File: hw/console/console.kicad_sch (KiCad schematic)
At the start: 155 parts, among them J1 Batt, J301 USB-C 16P, J401 DM3AT-SF-PEJM5, J501 SPK 8R, J601 FFC-40 0.5mm, J901 UART, Q601 AO3400A, SW1 Движок, SW101 UP, SW102 DOWN, SW103 LEFT, SW104 RIGHT, SW105 SELECT, SW106 START, SW107 A, SW108 B, SW109 C, SW110 D, U1 F133-A, U2 SY8089AAAC, U3 SY8089AAAC, U4 SY8089AAAC, U401 W25Q32JVSSIQ, U5 TP4056, U501 PAM8301, Y1 24 МГц, Y2 32.768 кГц

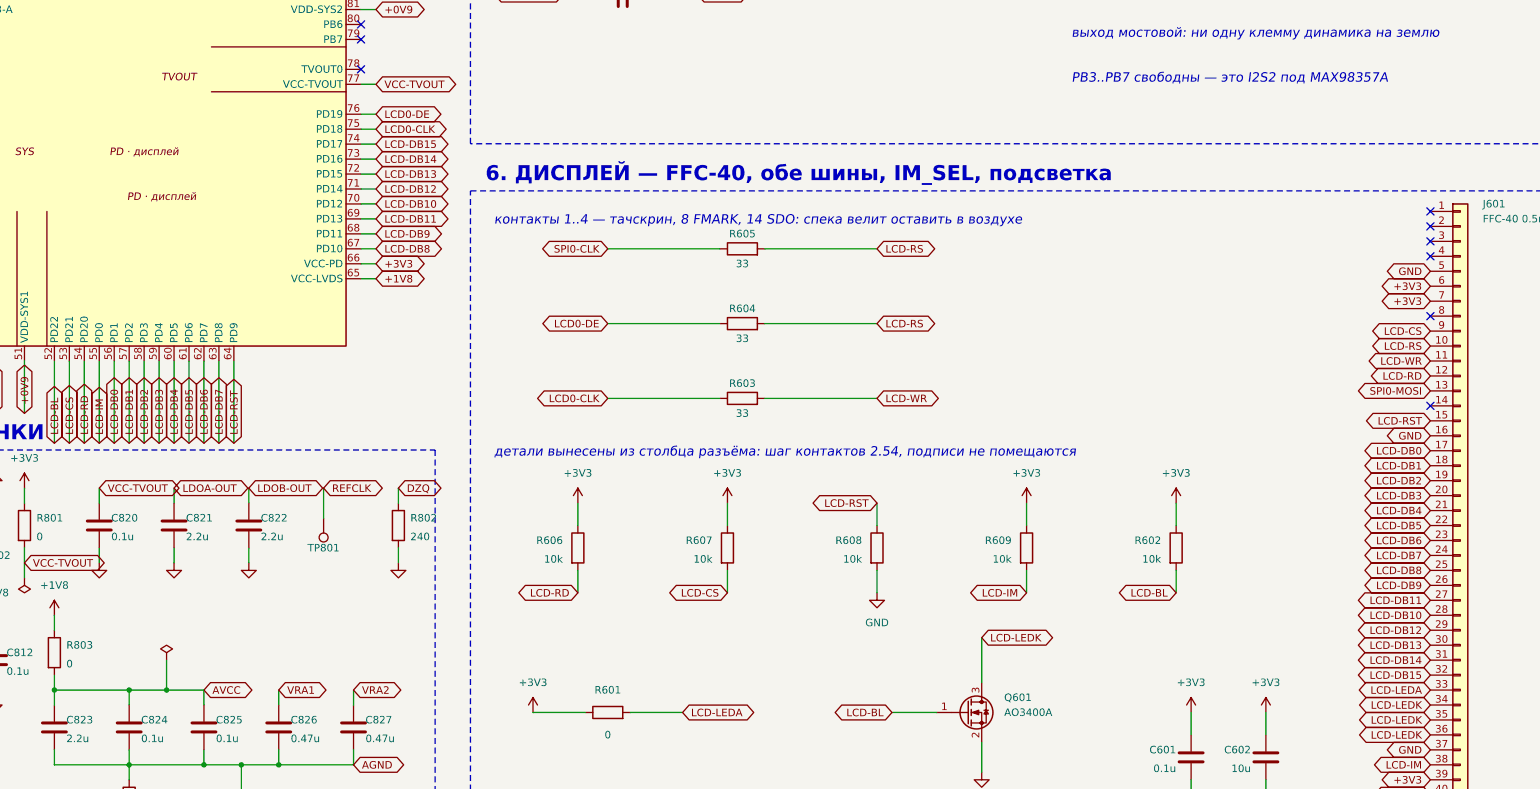
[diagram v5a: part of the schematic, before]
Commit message: hw: дисплей только по SPI — и такт приходил не на тот вывод
Главное: в `06-display.md §2.2` выводы 10 и 11 шлейфа были перепутаны, схема
KiCad это унаследовала, и `SPI0-CLK` заводился на вывод 10 — то есть ТАКТ
ПОПАДАЛ НА `D/C`. Плата бы не заработала.

Разобрано по схеме самого модуля (`docs/display/ili9488/3.5寸40P，9488原理图.pdf`,
файлы продавца): против выводов стоят функции `DCX/RS(SPI-4)` у 10 и
`WRX/SPI SCL` у 11. Колонки при извлечении текста разъезжаются, поэтому
сверено по семи проверяемым соседям — 8 `FMARK`, 12 `RDX`, 13 `SDA`, 14 `SDO`,
15 `RESX`, 16 `GND`, 17 `DB0`: вся цепочка совпала. Третий свидетель — рабочая
пайка проводами (AGENTS.md). Цепи теперь названы по ФУНКЦИИ (`LCD-SCL`,
`LCD-DC`), а не по шелкографии модуля: имя «WR» у тактового сигнала и есть та
ловушка, в которую схема попала.

Второе: `PE0` и `PE1` не были подключены вовсе — у платы не было ни `D/C`, ни
сброса дисплея.

Третье, механизм: блок схемы не убирал за собой. Зоны чистки строились по
тому, что он рисует СЕЙЧАС, поэтому снятый вывод их не получал и его прежние
отвод с меткой оставались навсегда — семнадцать цепей `LCD-DB*` висели
метками, а блок печатал «убрано 354, вставлено 354». Он убрал всё, что видел,
просто видел не всё. Зона чистки теперь на каждый вывод корпуса.

Параллельный интерфейс снят по решению заказчика (требование 4 ТЗ отменено):
кадр равен `max(эмуляция, передача)`, замер на железе даёт 29 мс против 2 мс,
то есть шина 8080 стоила бы самой тяжёлой задачи на плате ради пяти кадров.
`DB0`…`DB15` на землю, как требует спека для неиспользуемых линий.

`LCD-DC` на `PD15` (вывод 72) — выбран замером: 22.2 мм до вывода 10 разъёма и
перепад 0.2 мм, против 32.0 мм у `PE0` с заходом на тесную сторону корпуса.
Прошивку пока НЕ трогаем, она должна работать на проводном прототипе; что
менять на плате v2 — записано у самой строки в `main.rs`, включая то, что `CS`
дисплея придётся дёргать вручную: `SPI0-CS0` занят флешкой.

`pcb00_nets.py` научился заводить новые цепи — это был п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
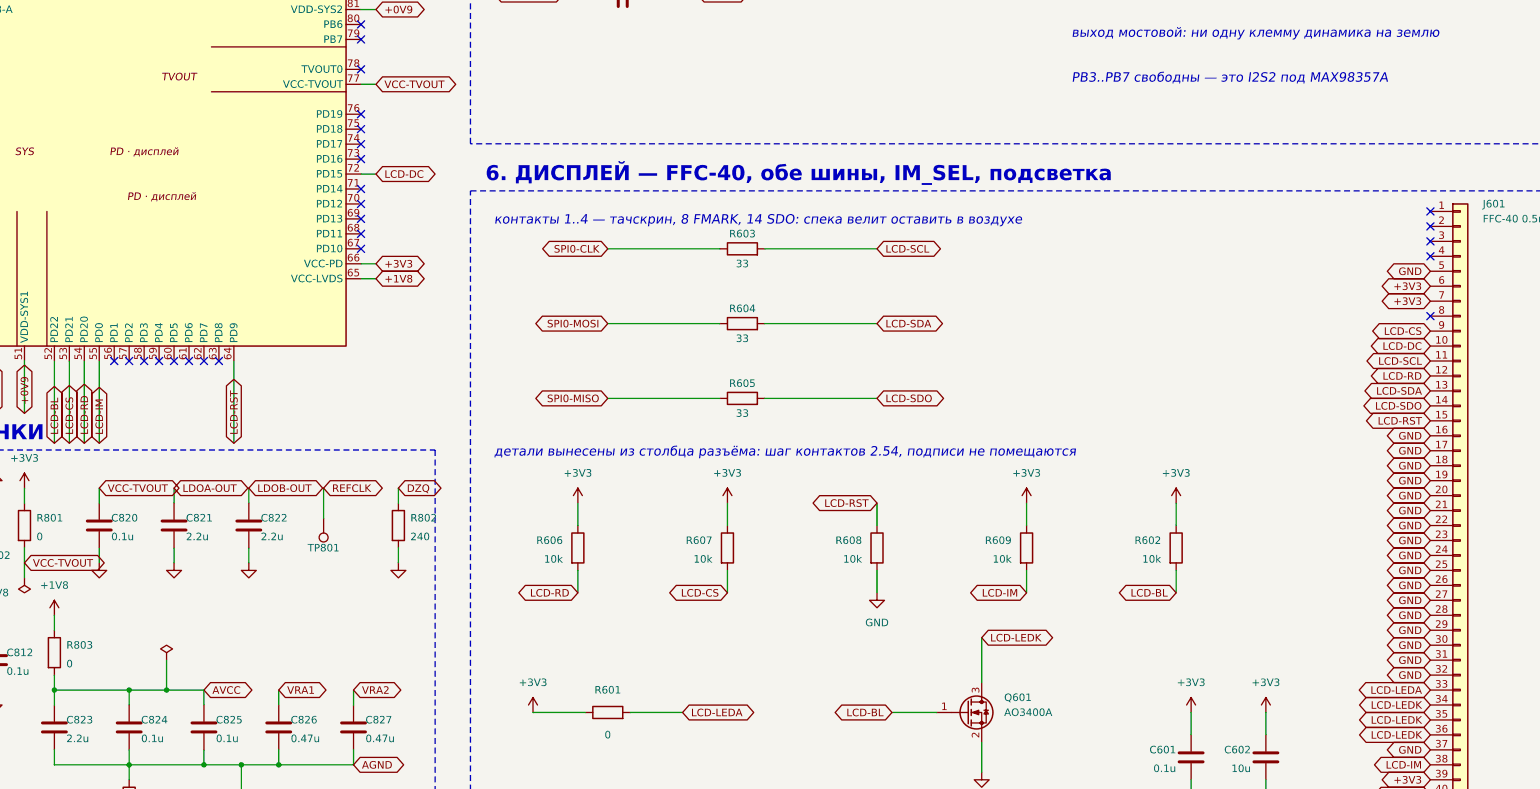
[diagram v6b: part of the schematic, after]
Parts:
- R604, R605: Источник 06-display.md §6.3 -> 06-display.md §6.4
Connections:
- net GND: now also J601.17 (Pin_17), J601.18 (Pin_18), J601.19 (Pin_19), J601.20 (Pin_20), J601.21 (Pin_21), J601.22 (Pin_22), J601.23 (Pin_23), J601.24 (Pin_24), J601.25 (Pin_25), J601.26 (Pin_26), J601.27 (Pin_27), J601.28 (Pin_28), J601.29 (Pin_29), J601.30 (Pin_30), J601.31 (Pin_31), J601.32 (Pin_32)
- net SPI0-CLK: now also R603.1; no longer R605.1
- net SPI0-MISO: now also R605.1
- net SPI0-MOSI: now also R604.1; no longer J601.13 (Pin_13)
- net LCD-SDO: now reaches J601.14 (Pin_14)
- net LCD-SDO: now also R605.2
- net LCD-DB0: no longer names the net of U1.56 (PD1)
- net LCD-DB0: no longer J601.17 (Pin_17)
- net LCD-DB1: no longer names the net of U1.57 (PD2)
- net LCD-DB1: no longer J601.18 (Pin_18)
- net LCD-DB10: no longer names the net of U1.70 (PD12)
- net LCD-DB10: no longer J601.28 (Pin_28)
- net LCD-DB11: no longer names the net of U1.69 (PD13)
- net LCD-DB11: no longer J601.27 (Pin_27)
- net LCD-DB12: no longer names the net of U1.71 (PD14)
- net LCD-DB12: no longer J601.29 (Pin_29)
- net LCD-DB13 renamed LCD-DC
- net LCD-DC: now also J601.10 (Pin_10); no longer J601.30 (Pin_30)
- net LCD-DB14: no longer names the net of U1.73 (PD16)
- net LCD-DB14: no longer J601.31 (Pin_31)
- net LCD-DB15: no longer names the net of U1.74 (PD17)
- net LCD-DB15: no longer J601.32 (Pin_32)
- net LCD-DB2: no longer names the net of U1.58 (PD3)
- net LCD-DB2: no longer J601.19 (Pin_19)
- net LCD-DB3: no longer names the net of U1.59 (PD4)
- net LCD-DB3: no longer J601.20 (Pin_20)
- net LCD-DB4: no longer names the net of U1.60 (PD5)
- net LCD-DB4: no longer J601.21 (Pin_21)
- net LCD-DB5: no longer names the net of U1.61 (PD6)
- net LCD-DB5: no longer J601.22 (Pin_22)
- net LCD-DB6: no longer names the net of U1.62 (PD7)
- net LCD-DB6: no longer J601.23 (Pin_23)
- net LCD-DB7: no longer names the net of U1.63 (PD8)
- net LCD-DB7: no longer J601.24 (Pin_24)
- net LCD-DB8: no longer names the net of U1.67 (PD10)
- net LCD-DB8: no longer J601.25 (Pin_25)
- net LCD-DB9: no longer names the net of U1.68 (PD11)
- net LCD-DB9: no longer J601.26 (Pin_26)
- removed net LCD-RS: J601.10 (Pin_10), R604.2, R605.2
- net LCD-WR renamed LCD-SCL
- net LCD0-CLK: no longer names the net of U1.75 (PD18)
- net LCD0-CLK: no longer R603.1
- net LCD0-DE: no longer names the net of U1.76 (PD19)
- net LCD0-DE: no longer R604.1
- new net LCD-SDA: J601.13 (Pin_13), R604.2
- no-connect marks 41 -> 57
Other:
- moved on the sheet: R603, R605

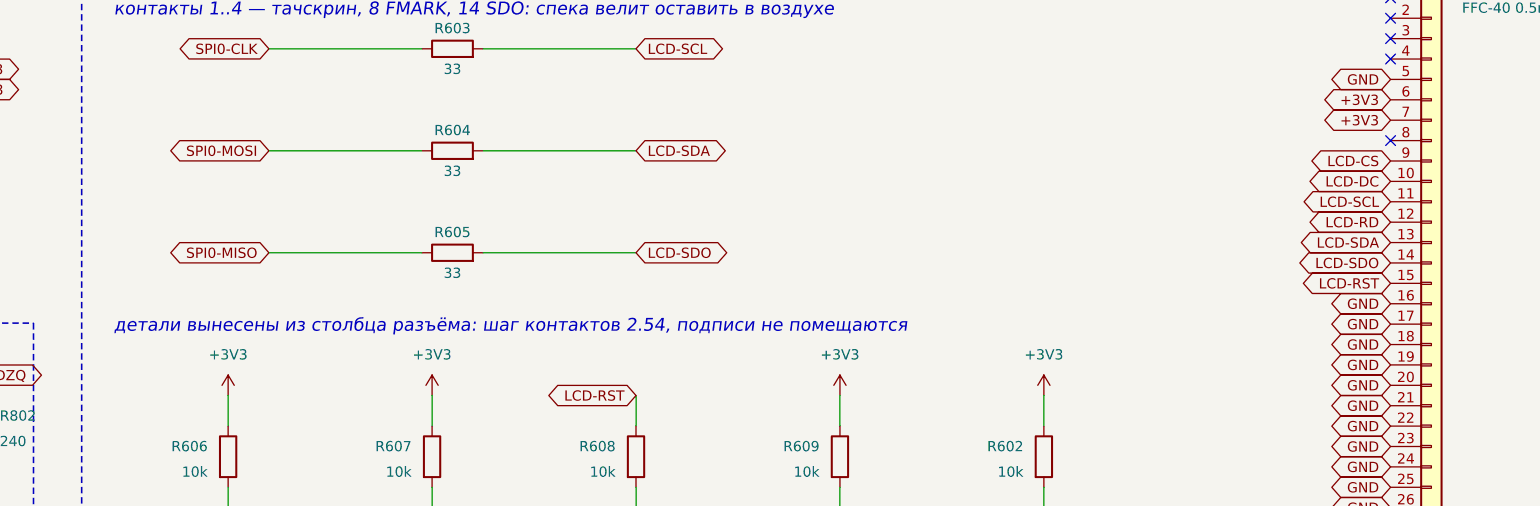
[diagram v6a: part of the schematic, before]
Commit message: hw: `SDO` не подключаем — я переопределил решение, и это стоило 266 мм
И спека панели («If not used, open this pin»), и инструкция продавца
(«14PIN_SDO — в воздухе»), и наш же §6.1 говорили: не подключать. Я завёл
`SDO` на `SPI0-MISO` ради удобной проверки при первом запуске — код умеет
`read_id`, и прочитать идентификатор панели это лучший способ убедиться, что
она отвечает.

Цена вскрылась замером длины цепей: `SPI0-MISO` стала ВТОРОЙ по длине цепью
платы, 266 мм. Вся длина — отвод на шине, которую делит ЗАГРУЗОЧНАЯ флешка.
Если `SDO` дисплея не уходит в высокий импеданс при снятом `CS` — у
контроллеров ILI это известная болезнь, и спека об этом молчит, — флешка не
прочитается и плата не загрузится вовсе. Менять «читается ли дисплей» на
«загружается ли плата» нельзя. Откачено, `R605` с платы убран.

Таблица §6.1 несла те же перепутанные выводы 10 и 11, что и §2.2, — из неё
ошибка и расходилась. Исправлена, добавлен §6.1.1 с разбором `SDO` и
предупреждение продавца красным: «3.5寸TFT不建议用串口驱动», для 3.5″ панели
последовательный интерфейс не рекомендуется. Запрет не абсолютный (проводной
прототип даёт 33 кадра по SPI на 50 МГц), но при странном поведении панели это
первый подозреваемый.

Сводка круга больше не врёт нулём: медь считается ПО ПЛАТЕ, а не по последнему
заходу добора. Последний заход кладёт ноль отрезков — тем он и кончается, — и
«переходных 0» на разведённой плате читалось как «ничего не вышло».

Co-Authored-By: Claude Opus 5 (1M context) <noreply@anthropic.com>
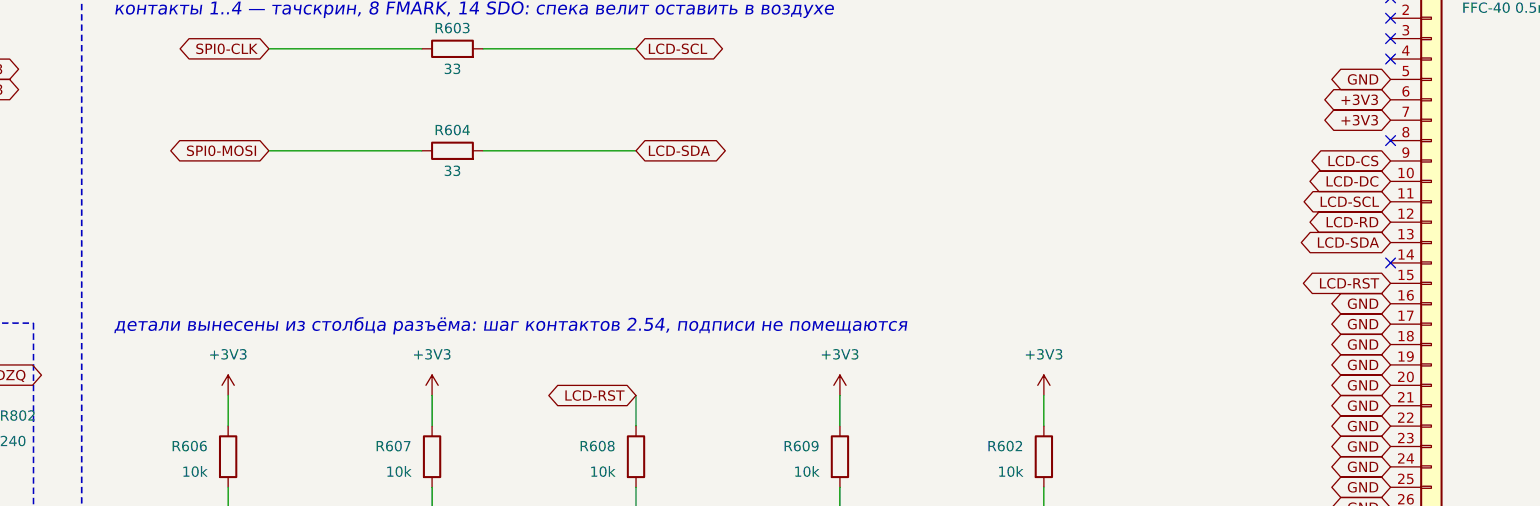
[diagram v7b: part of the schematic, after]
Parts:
- removed R605: 33, Resistor_SMD:R_0805_2012Metric_Pad1.20x1.40mm_HandSolder, symbol Device:R
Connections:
- net LCD-SDO: no longer names the net of J601.14 (Pin_14)
- no-connect marks 57 -> 58

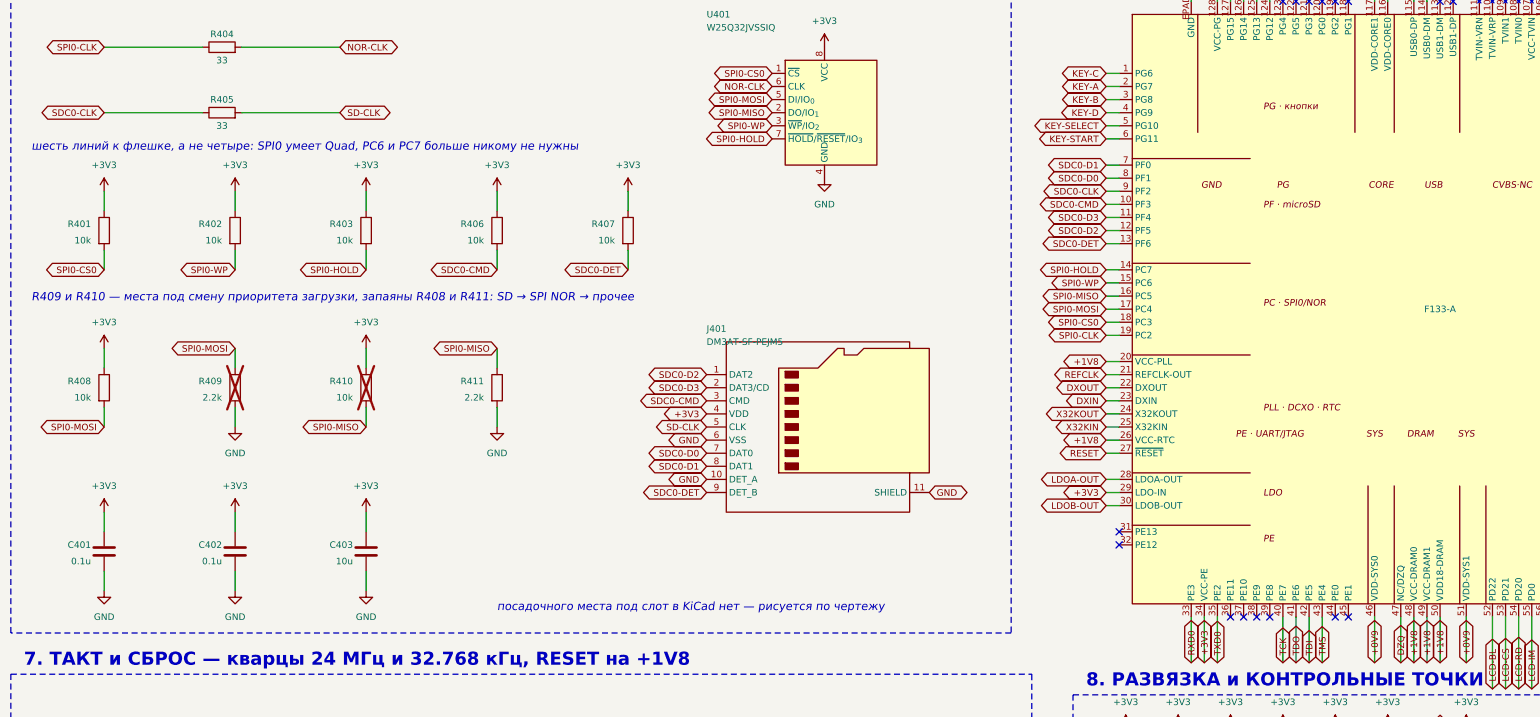
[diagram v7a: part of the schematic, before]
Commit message: hw: карты памяти в первой ревизии нет
Решение заказчика, подтверждённое числом: снятие карты убирает 8 неразведённых
связей из 61 — больше, чем дала любая правка размещения. Дело не столько в её
семи цепях, сколько в зоне запрета меди под лотком `DM3AT` (каталог Hirose,
стр. 3): она вырезает дыру в ОБОИХ слоях посреди самой тесной части платы.

Играть это не мешает: ПЗУ игры вшито в прошивку (`include_bytes!` в
`nes/cart.rs`), а сама прошивка пишется в SPI-флешку через `xfel spinor write`
— один раз с компьютера, дальше плата стартует сама. Флешку поэтому и
оставили: по разводке она стоит трёх связей, а самостоятельность даёт.

Обвязки у карты ШЕСТЬ деталей, а не четыре, и это поймал заказчик, а не
проверка: кроме `J401`, `R405`, `R406`, `R407` ей принадлежат `C402` 0.1 мкФ и
`C403` 10 мкФ — оба на её питании, но лежат они не среди «деталей карты», а в
общей развязке блока. Значит цифра 8 связей была занижена: эти два конденсатора
висят на `+3V3`, то есть на цепи с наибольшим числом разрывов.

Деталей на плате 155 -> 148. ERC 0, своя проверка 0 из 16.

Незакрытый хвост, записан в коде: образ с заголовком `boot0` мы не собираем —
грузимся через `xfel exec`, которому заголовок не нужен. Железо к загрузке с
флешки готово, шаг в прошивке — нет.

Заодно: `pcb09_gnd.py` научился подводить ДОРОЖКУ к куску заливки, куда не
влезла заклёпка (в одном таком сидит земляной вывод `U501` — то есть без этого
у усилителя земля висит в воздухе); порог проверки развязки поднят с 7 до 12 мм
по замеру референса (у Xassette развязка стоит в 5.5…22 мм, то есть 7 было
строже живой практики, и десять вечных нарушений приучали не смотреть в
отчёт); контур `J601` в библиотеке приведён к тому же виду, что на плате.

Co-Authored-By: Claude Opus 5 (1M context) <noreply@anthropic.com>
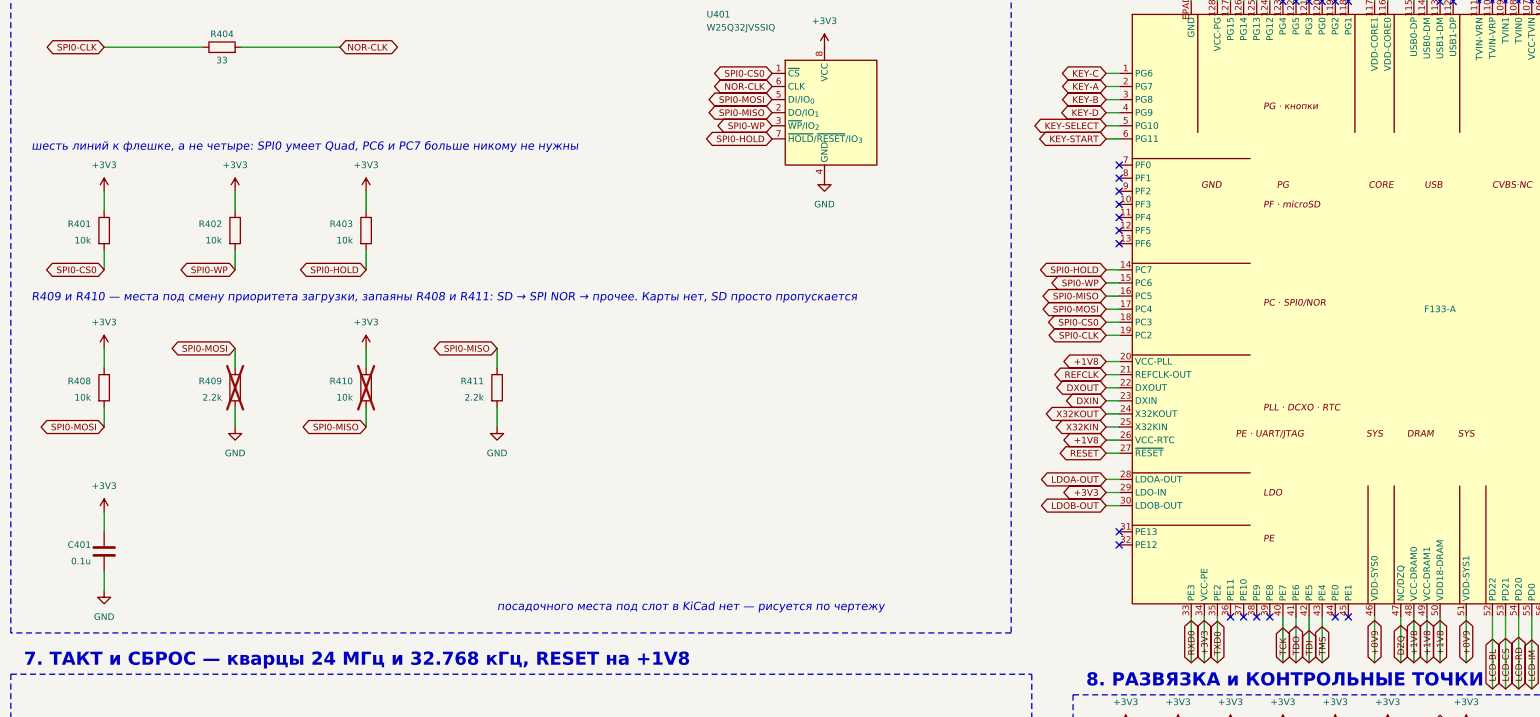
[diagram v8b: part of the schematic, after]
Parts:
- removed C402: 0.1u, Capacitor_SMD:C_0805_2012Metric_Pad1.18x1.45mm_HandSolder, symbol Device:C
- removed C403: 10u, Capacitor_SMD:C_0805_2012Metric_Pad1.18x1.45mm_HandSolder, symbol Device:C
- removed J401: DM3AT-SF-PEJM5, Connector_Card:microSD_HC_Hirose_DM3AT-SF-PEJM5, symbol Connector:Micro_SD_Card_Det_Hirose_DM3AT
- removed R405: 33, Resistor_SMD:R_0805_2012Metric_Pad1.20x1.40mm_HandSolder, symbol Device:R
- removed R406, R407: 10k, Resistor_SMD:R_0805_2012Metric_Pad1.20x1.40mm_HandSolder, symbol Device:R
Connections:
- net SDC0-CLK: no longer names the net of U1.9 (PF2)
- net SDC0-CMD: no longer names the net of U1.10 (PF3)
- net SDC0-D0: no longer names the net of U1.8 (PF1)
- net SDC0-D1: no longer names the net of U1.7 (PF0)
- net SDC0-D2: no longer names the net of U1.12 (PF5)
- net SDC0-D3: no longer names the net of U1.11 (PF4)
- net SDC0-DET: no longer names the net of U1.13 (PF6)
- no-connect marks 58 -> 65
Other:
- note added: "R409 и R410 — места под смену приоритета загрузки, запаяны R408 и R411: SD → SPI NOR → прочее. Карты нет, SD просто пропускается"
- note removed: "R409 и R410 — места под смену приоритета загрузки, запаяны R408 и R411: SD → SPI NOR → прочее"
